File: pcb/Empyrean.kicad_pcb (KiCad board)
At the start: 2 copper layers, 18.3 x 45.6 mm, 50 parts, among them J1 FCI 10118194-0001LF, J2 Harwin M50-3500542, J3 SPI, J4 CONN_01X15, J5 CONN_01X15, Q1 DMG1012UW-7, Q2 DMG1013T-7, Q3 DMG1013T-7, Q4 DMG1012UW-7, U1 LP2985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

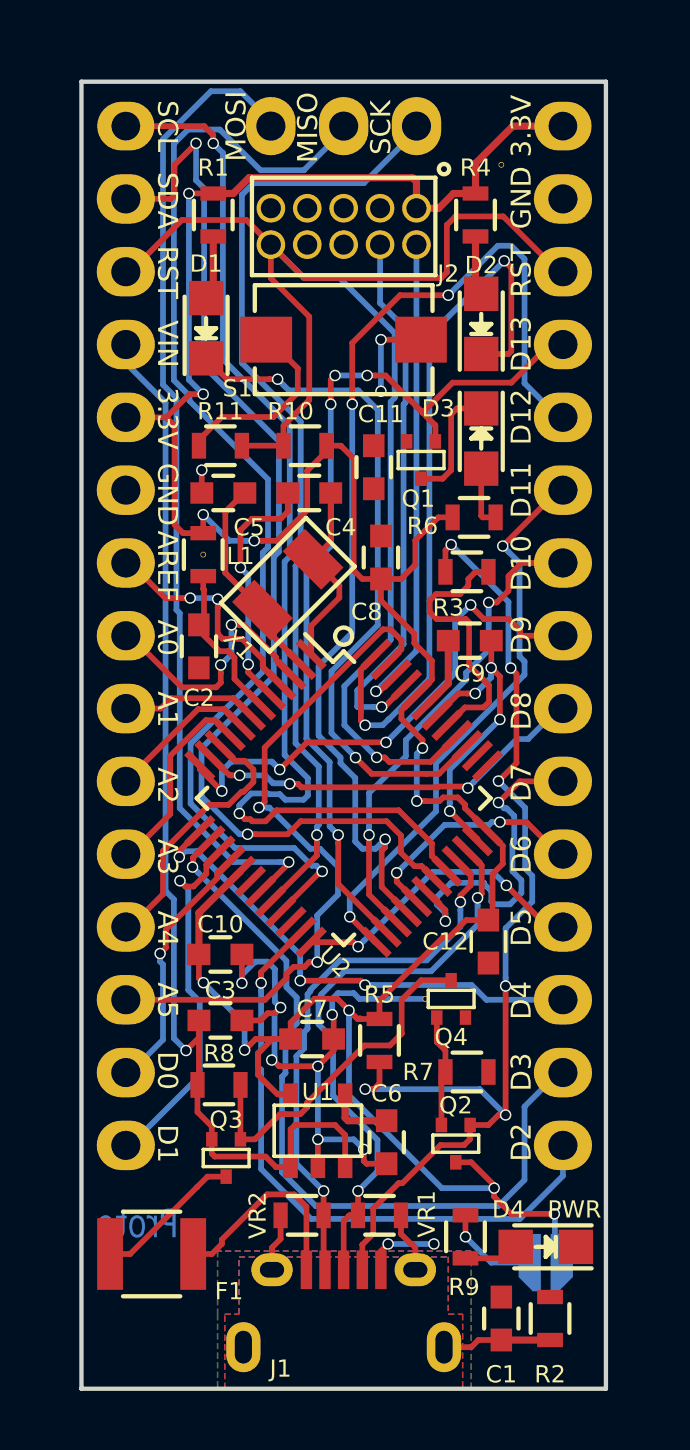
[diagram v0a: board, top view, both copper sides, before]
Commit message: Updated PCB with castellation
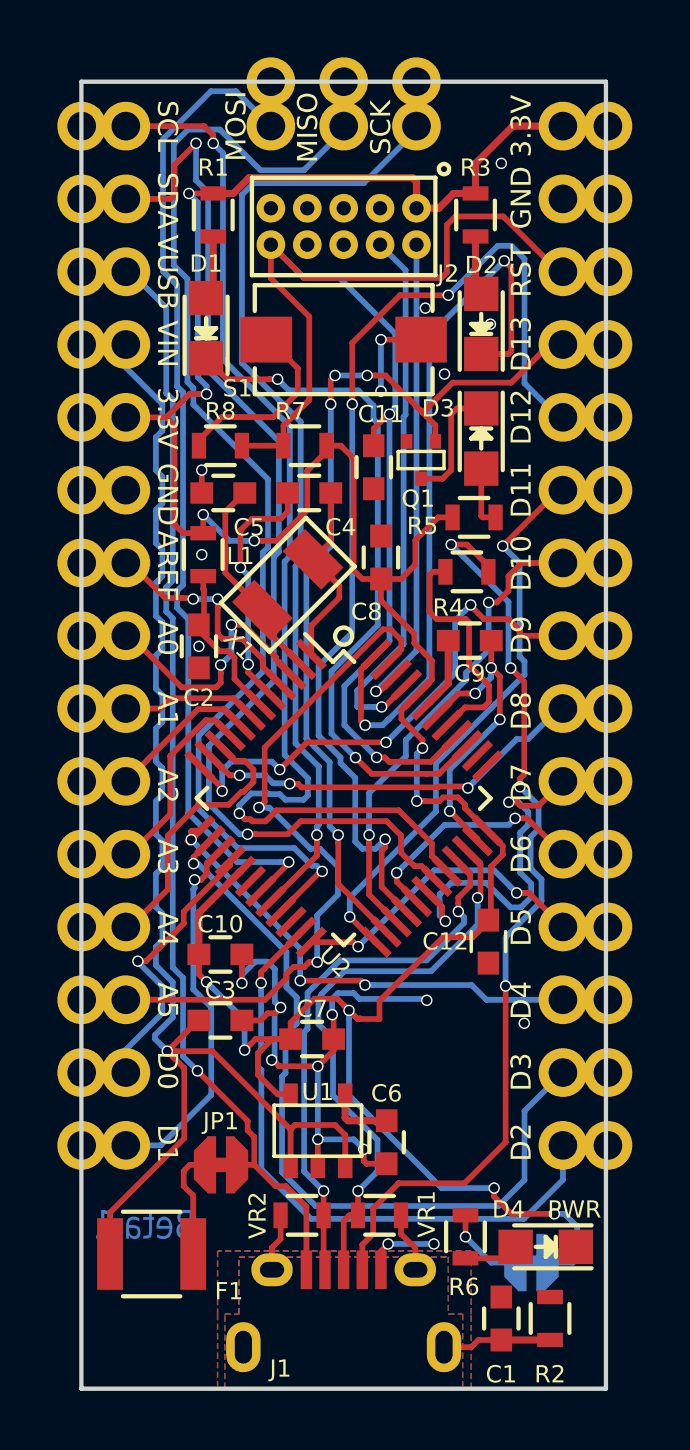
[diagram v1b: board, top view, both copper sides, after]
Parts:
- removed Q2, Q3: DMG1013T-7, EtherkitKicadLibrary:SOT523
- removed Q4: DMG1012UW-7, EtherkitKicadLibrary:SOT523
- removed the R5 at (135.4, 133.4)
- removed the R7 at (138.4, 134.6)
- removed the R8 at (129.8, 135.0)
- removed VIA (x3): VAL**, EtherkitKicadLibrary:VIA
- added JP2: Power LED Enable, EtherkitKicadLibrary:SOLDER_JUMPER_NC, B.Cu at (140.7, 141.2)
- added REF**: PinHeader_1x15_P2.54mm_Vertical_Unkeyed, EtherkitKicadLibrary:PinHeader_1x15_P2.54mm_Vertical_Unkeyed, F.Cu at (125.0, 101.5)
- added REF**: PinHeader_1x15_P2.54mm_Vertical_Unkeyed, EtherkitKicadLibrary:PinHeader_1x15_P2.54mm_Vertical_Unkeyed, F.Cu at (143.4, 101.5)
- added REF**: PinHeader_1x03_P2.54mm_Vertical_Unkeyed, EtherkitKicadLibrary:PinHeader_1x03_P2.54mm_Vertical_Unkeyed, F.Cu at (131.6, 100.0)
- J3: footprint EtherkitKicadLibrary:Pin_Header_Straight_1x03_NoBorder -> EtherkitKicadLibrary:PinHeader_1x03_P2.54mm_Vertical_Unkeyed
- J4, J5: footprint EtherkitKicadLibrary:Pin_Header_Straight_1x15_NoBorder -> EtherkitKicadLibrary:PinHeader_1x15_P2.54mm_Vertical_Unkeyed
- JP1: value Power LED Enable -> VUSB Disable; footprint EtherkitKicadLibrary:SOLDER_JUMPER -> EtherkitKicadLibrary:SOLDER_JUMPER_NC; moved to F.Cu
- Q1: value DMG1012UW-7 -> DMG1012T-7
- moved JP1 11.8 mm to (129.9, 137.8)
- renumbered R4 to R3, R3 to R4, R6 to R5, R9 to R6, R10 to R7, R11 to R8
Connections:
- F1 pad 2: Net-(F1-Pad2) -> VIN
- J1 pad 1: Net-(F1-Pad1) -> VUSB
- J4 pad 3: RESET -> VUSB
- JP1 pad 1: +3.3V -> VUSB
- JP1 pad 2: Net-(JP1-Pad2) -> Net-(F1-Pad1)
- R4 pad 1: Net-(J1-Pad4) -> USB_HOST_EN
- R4 pad 2: USB_HOST_EN -> Net-(J1-Pad4)
- R6 pad 1: Net-(JP1-Pad2) -> Net-(JP2-Pad2)
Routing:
- net VUSB: track 0.00 -> 38.5 mm, vias 0 -> 1
- net Net-(Q3-Pad2): track 12.3 -> 0.00 mm
- net VIN: track 39.1 -> 47.2 mm
- net Net-(J1-Pad4): track 38.2 -> 32.7 mm, vias 6 -> 4
- net Net-(F1-Pad2): track 5.17 -> 0.00 mm
- net RESET: track 53.7 -> 48.9 mm, vias 1 -> 2
- net Net-(Q2-Pad1): track 3.93 -> 0.00 mm
- net Net-(F1-Pad1): track 7.28 -> 3.64 mm
- net Net-(JP1-Pad2): track 3.22 -> 0.00 mm, vias 1 -> 0
- net Net-(JP2-Pad2): track 0.00 -> 2.64 mm, vias 0 -> 1
- net USB_HOST_EN: track 9.39 -> 8.28 mm
- net D4: track 17.7 -> 16.8 mm
- net D0/UART_RX: track 9.06 -> 9.76 mm
- net GND: vias 18 -> 26
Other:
- net class Default: clearance 0.18 -> 0.16
- rule trace_clearance: 0.18 -> 0.16
- board text added: "2019"
- board text added: "Beta 1"
- board text added: "VUSB"
- board text removed: "2017"
- board text removed: "Proto"

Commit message: Add Empyrean Quick Reference
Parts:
- added Ref**: Val**, EtherkitKicadLibrary:EtherkitLogoSmall, F.Cu at (138.2, 134.8)

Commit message: Set proper rev on documentation
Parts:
- JP1, JP2: footprint EtherkitKicadLibrary:SOLDER_JUMPER_NC -> EtherkitKicadLibrary:SOLDER_JUMPER
- moved J1 1.45 mm to (134.2, 144.2)
- turned D1 to 180 degrees
- turned D2 to 180 degrees
- turned D3 to 0 degrees
- turned D4 to 270 degrees
- turned Q1 to 180 degrees
- turned U1 to 90 degrees
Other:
- net class Default: clearance 0.16 -> 0.13
- rule trace_clearance: 0.16 -> 0.13
- rule trace_min: 0.18 -> 0.16
- rule via_min_size: 0.4 -> 0.3
- board text added: "2020"
- board text added: "Rev A"
- board text removed: "2019"
- board text removed: "Beta 1"
